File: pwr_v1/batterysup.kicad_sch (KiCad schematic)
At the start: 0 parts

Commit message: Schematic updated
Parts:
- added D3, D4, D5, D6, D7, D8: D, symbol Device:D
- added R1, R10, R11, R12, R13, R14, R4, R5, R6, R7, R8, R9: R_Small_US, symbol Device:R_Small_US
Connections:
- new net: D7.2 (A), R11.2, R12.2
- new net: D3.2 (A), R1.2, R4.2
- new net: D5.2 (A), R7.2, R8.2
- new net: D4.2 (A), R5.2, R6.2
- new net: D6.2 (A), R10.2, R9.2
- new net: D8.2 (A), R13.2, R14.2
- new net B1: R1.1
- new net B2: R5.1
- new net B3: R7.1
- new net B4: R9.1
- new net B5: R11.1
- new net B6: R13.1
- new net G: R10.1, R12.1, R14.1, R4.1, R6.1, R8.1
- new net O1: D3.1 (K)
- new net O2: D4.1 (K)
- new net O3: D5.1 (K)
- new net O4: D6.1 (K)
- new net O5: D7.1 (K)
- new net O6: D8.1 (K)

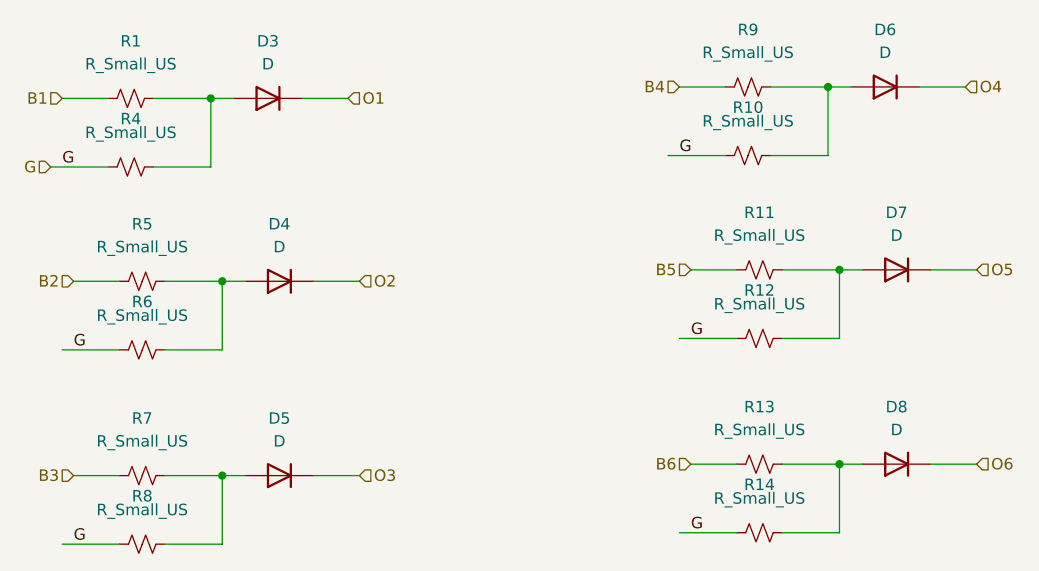
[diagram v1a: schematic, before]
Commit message: Sch and Layout updated; Added batt sup ckt, placed and routed all motor drivers.
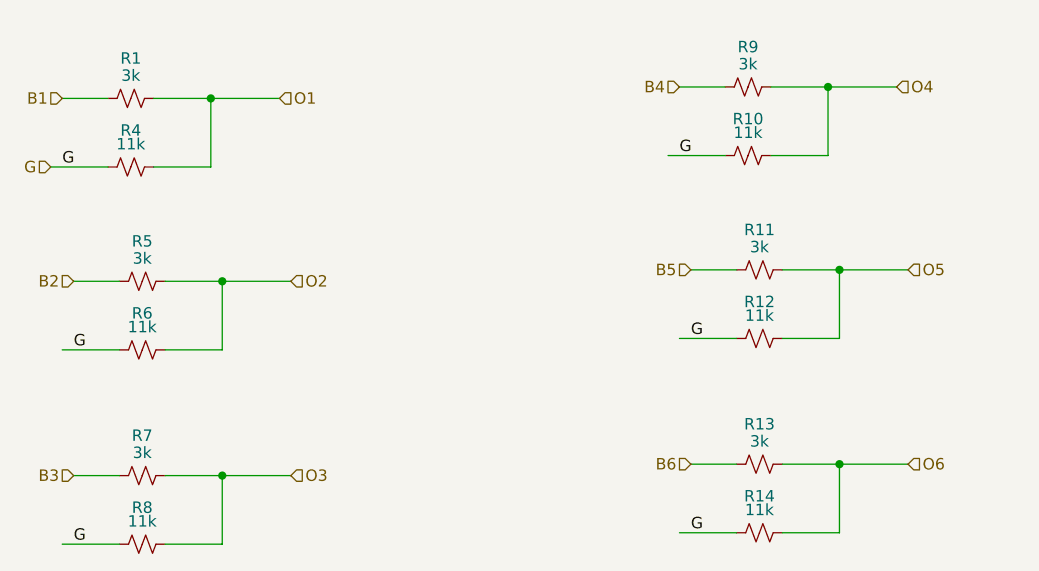
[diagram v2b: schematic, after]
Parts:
- removed D3, D4, D5, D6, D7, D8: D, symbol Device:D
- R1, R11, R13, R5, R7, R9: value R_Small_US -> 3k; footprint (none) -> Resistor_SMD:R_0402_1005Metric
- R10, R12, R14, R4, R6, R8: value R_Small_US -> 11k; footprint (none) -> Resistor_SMD:R_0402_1005Metric
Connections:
- net O1: now also R1.2, R4.2
- net O2: now also R5.2, R6.2
- net O3: now also R7.2, R8.2
- net O4: now also R10.2, R9.2
- net O5: now also R11.2, R12.2
- net O6: now also R13.2, R14.2

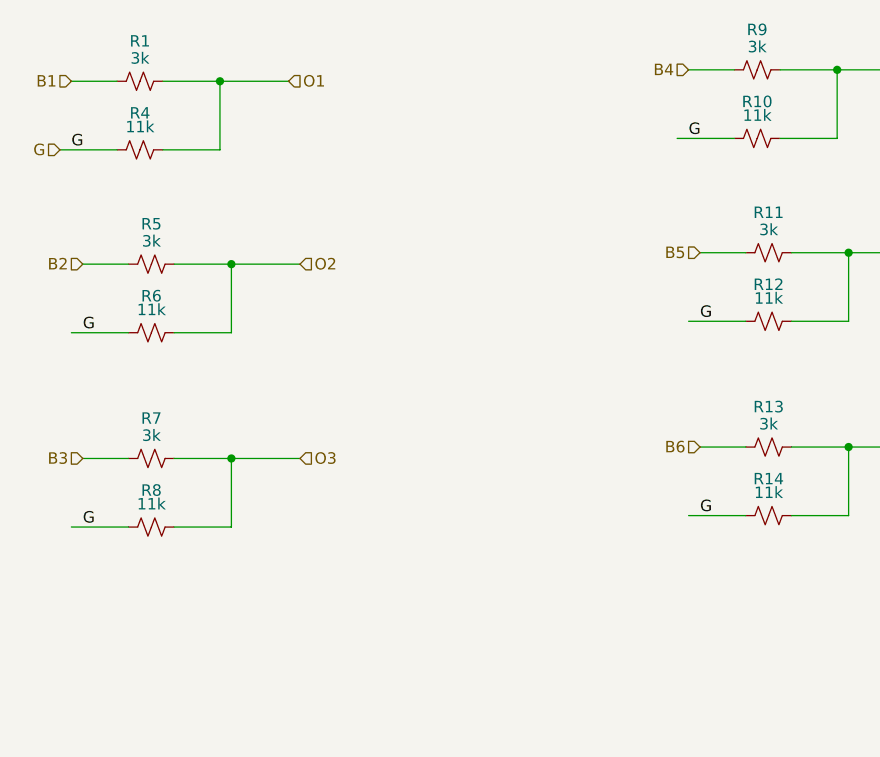
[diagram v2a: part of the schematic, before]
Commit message: Schematic and layout updated; Layout placement and routing completed
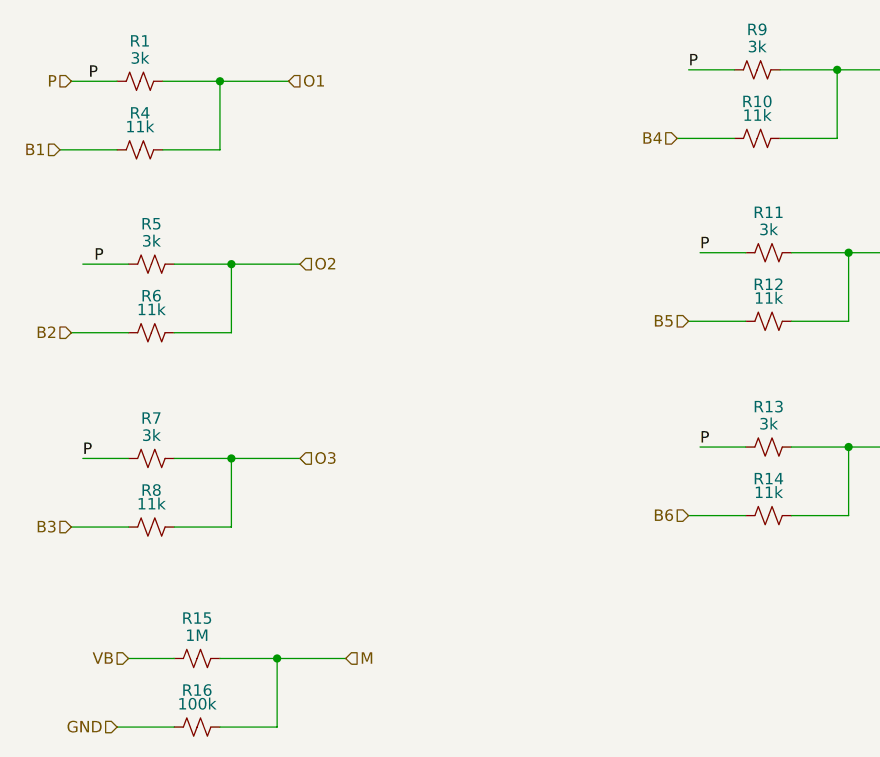
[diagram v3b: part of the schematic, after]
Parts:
- added R15: 1M, Resistor_SMD:R_0603_1608Metric, symbol Device:R_Small_US
- added R16: 100k, Resistor_SMD:R_0603_1608Metric, symbol Device:R_Small_US
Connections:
- net B1: now also R4.1; no longer R1.1
- net B2: now also R6.1; no longer R5.1
- net B3: now also R8.1; no longer R7.1
- net B4: now also R10.1; no longer R9.1
- net B5: now also R12.1; no longer R11.1
- net B6: now also R14.1; no longer R13.1
- removed net G: R10.1, R12.1, R14.1, R4.1, R6.1, R8.1
- new net GND: R16.1
- new net M: R15.2, R16.2
- new net P: R1.1, R11.1, R13.1, R5.1, R7.1, R9.1
- new net VB: R15.1

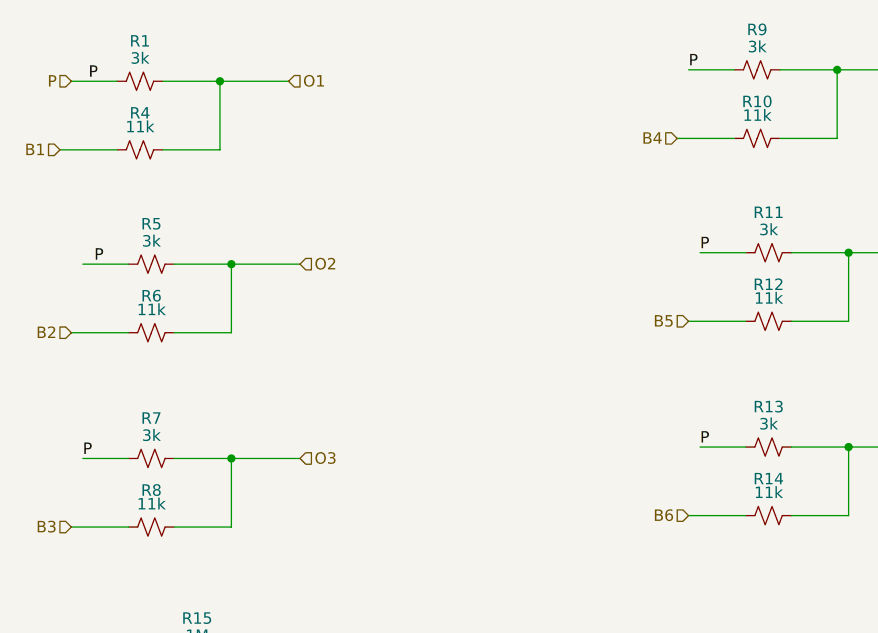
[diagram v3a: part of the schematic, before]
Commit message: Battery monitoring circuit updated; 1cm keepout added on front of board
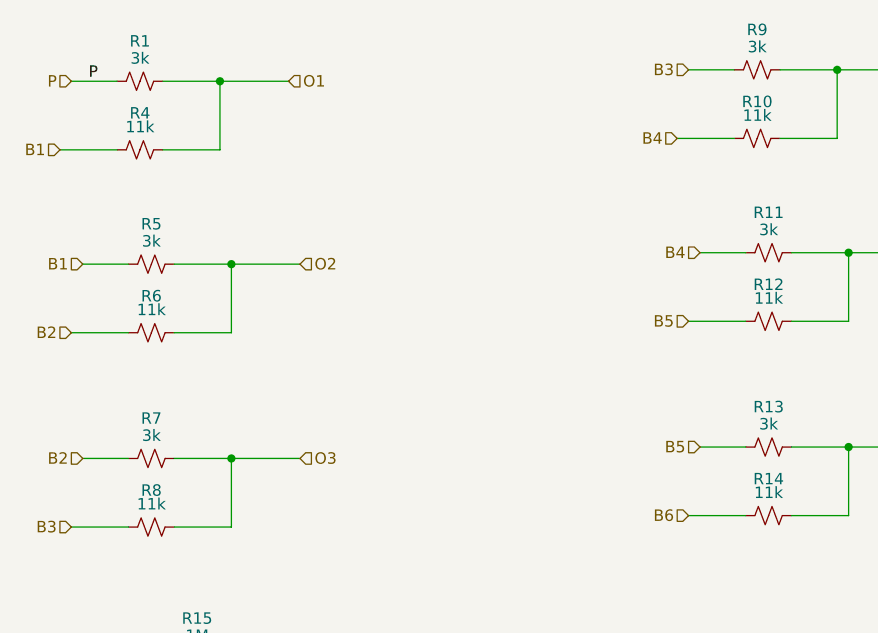
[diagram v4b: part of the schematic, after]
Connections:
- net B1: now also R5.1
- net B2: now also R7.1
- net B3: now also R9.1
- net B4: now also R11.1
- net B5: now also R13.1
- net P: no longer R11.1, R13.1, R5.1, R7.1, R9.1
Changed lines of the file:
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@@
-		)
-	)
-	(label "P"
-		(at 115.57 52.07 0)
-		(fields_autoplaced yes)
-		(effects
-			(font
-				(size 1.27 1.27)
-			)
-			(justify left bottom)
-		)
-	)
-	(label "P"
-		(at 46.99 74.93 0)
-		(fields_autoplaced yes)
-		(effects
-			(font
-				(size 1.27 1.27)
-			)
-			(justify left bottom)
-		)
-	)
-	(label "P"
-		(at 115.57 73.66 0)
-		(fields_autoplaced yes)
-		(effects
-			(font
-				(size 1.27 1.27)
-			)
-			(justify left bottom)
-		)
-	)
-	(label "P"
-		(at 114.3 31.75 0)
-		(fields_autoplaced yes)
-		(effects
-			(font
-				(size 1.27 1.27)
-			)
-			(justify left bottom)
-		)
-	)
-	(label "P"
-		(at 48.26 53.34 0)
-		(fields_autoplaced yes)
-		(effects
-			(font
-				(size 1.27 1.27)
-			)
-			(justify left bottom)
 		)
 	)
@@
 		)
 	)
+	(hierarchical_label "B5"
+		(shape input)
+		(at 115.57 73.66 180)
+		(fields_autoplaced yes)
+		(effects
+			(font
+				(size 1.27 1.27)
+			)
+			(justify right)
+		)
+	)
 	(hierarchical_label "B4"
 		(shape input)
@@
 		)
 	)
+	(hierarchical_label "B2"
+		(shape input)
+		(at 46.99 74.93 180)
+		(fields_autoplaced yes)
+		(effects
+			(font
+				(size 1.27 1.27)
+			)
+			(justify right)
+		)
+	)
+	(hierarchical_label "B1"
+		(shape input)
+		(at 46.99 53.34 180)
+		(fields_autoplaced yes)
+		(effects
+			(font
+				(size 1.27 1.27)
+			)
+			(justify right)
+		)
+	)
 	(hierarchical_label "B5"
 		(shape input)
@@
 		)
 	)
+	(hierarchical_label "B3"
+		(shape input)
+		(at 114.3 31.75 180)
+		(fields_autoplaced yes)
+		(effects
+			(font
+				(size 1.27 1.27)
+			)
+			(justify right)
+		)
+	)
 	(hierarchical_label "P"
 		(shape input)
@@
 		)
 	)
+	(hierarchical_label "B4"
+		(shape input)
+		(at 115.57 52.07 180)
+		(fields_autoplaced yes)
+		(effects
+			(font
+				(size 1.27 1.27)
+			)
+			(justify right)
+		)
+	)

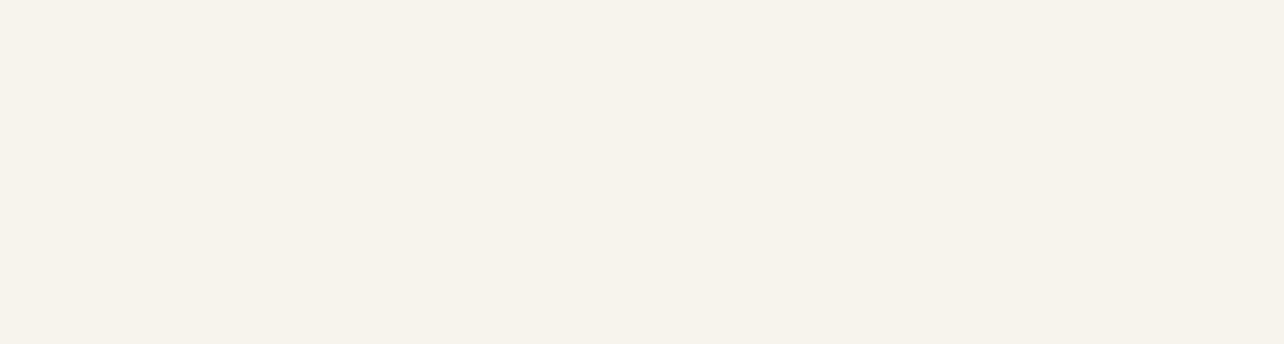
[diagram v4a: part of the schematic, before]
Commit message: File structure enhanced.
Added uniform titleblocks and 3D renders for easier view, file cleanups.
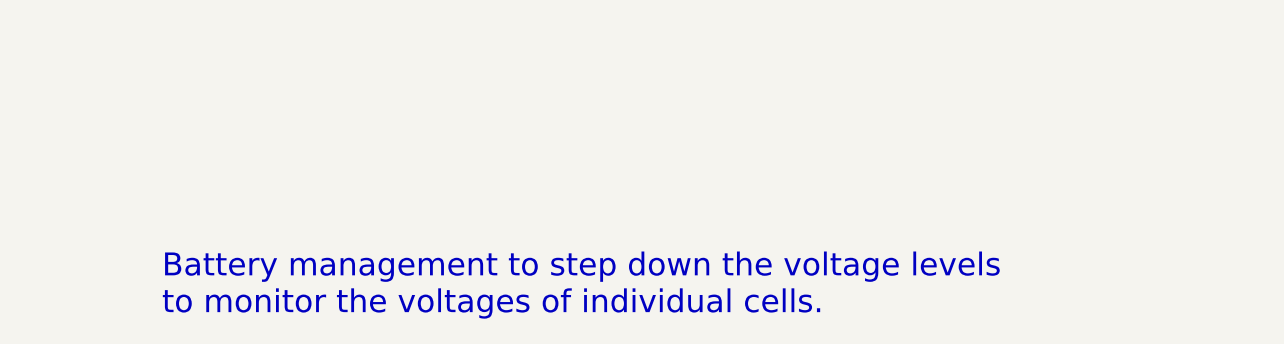
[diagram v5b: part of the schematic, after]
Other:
- note added: "Battery management to step down the voltage levels to monitor the voltages of individual cells."
- title: (none) -> Power board
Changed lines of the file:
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@@
 (kicad_sch
-	(version 20231120)
+	(version 20250114)
 	(generator "eeschema")
-	(generator_version "8.0")
-	(paper "A5")
+	(generator_version "9.0")
+	(paper "A4")
+	(title_block
+		(title "Power board")
+		(date "06-08-2024")
+		(rev "1")
+	)
+	(text "Battery management to step down the voltage levels \nto monitor the voltages of individual cells."
+		(exclude_from_sim no)
+		(at 195.58 168.275 0)
+		(effects
+			(font
+				(face "Gidole")
+				(size 2.54 2.54)
+			)
+			(justify left)
+		)
+	)
 	(junction
 		(at 130.81 31.75)
@@
 	(label "P"
 		(at 47.625 33.02 0)
-		(fields_autoplaced yes)
 		(effects
 			(font
@@
 		(shape input)
 		(at 50.8 104.775 180)
-		(fields_autoplaced yes)
 		(effects
 			(font
@@
 		(shape input)
 		(at 115.57 73.66 180)
-		(fields_autoplaced yes)
 		(effects
 			(font
@@
 		(shape input)
 		(at 113.03 39.37 180)
-		(fields_autoplaced yes)
 		(effects
 			(font
@@
 		(shape input)
 		(at 138.43 31.75 0)
-		(fields_autoplaced yes)
 		(effects
 			(font
@@
 		(shape input)
 		(at 76.2 97.155 0)
-		(fields_autoplaced yes)
 		(effects
 			(font
@@
 		(shape input)
 		(at 139.7 73.66 0)
-		(fields_autoplaced yes)
 		(effects
 			(font
@@
 		(shape input)
 		(at 71.12 74.93 0)
-		(fields_autoplaced yes)
 		(effects
 			(font
@@
 		(shape input)
 		(at 69.85 33.02 0)
-		(fields_autoplaced yes)
 		(effects
 			(font
@@
 		(shape input)
 		(at 46.99 74.93 180)
-		(fields_autoplaced yes)
 		(effects
 			(font
@@
 		(shape input)
 		(at 46.99 53.34 180)
-		(fields_autoplaced yes)
 		(effects
 			(font
@@
 		(shape input)
 		(at 114.3 59.69 180)
-		(fields_autoplaced yes)
 		(effects
 			(font
@@
 		(shape input)
 		(at 114.3 81.28 180)
-		(fields_autoplaced yes)
 		(effects
 			(font
@@
 		(shape input)
 		(at 71.12 53.34 0)
-		(fields_autoplaced yes)
 		(effects
 			(font
@@
 		(shape input)
 		(at 114.3 31.75 180)
-		(fields_autoplaced yes)
 		(effects
 			(font
@@
 		(shape input)
 		(at 45.72 33.02 180)
-		(fields_autoplaced yes)
 		(effects
 			(font
@@
 		(shape input)
 		(at 44.45 40.64 180)
-		(fields_autoplaced yes)
 		(effects
 			(font
@@
 		(shape input)
 		(at 45.72 60.96 180)
-		(fields_autoplaced yes)
 		(effects
 			(font
@@
 		(shape input)
 		(at 45.72 82.55 180)
-		(fields_autoplaced yes)
 		(effects
 			(font
@@
 		(shape input)
 		(at 52.07 97.155 180)
-		(fields_autoplaced yes)
 		(effects
 			(font
@@
 		(shape input)
 		(at 139.7 52.07 0)
-		(fields_autoplaced yes)
 		(effects
 			(font
@@
 		(shape input)
 		(at 115.57 52.07 180)
-		(fields_autoplaced yes)
-		(effects
-			(font
+		(effects
+			(font
